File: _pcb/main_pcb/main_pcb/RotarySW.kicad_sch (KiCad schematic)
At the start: 28 parts

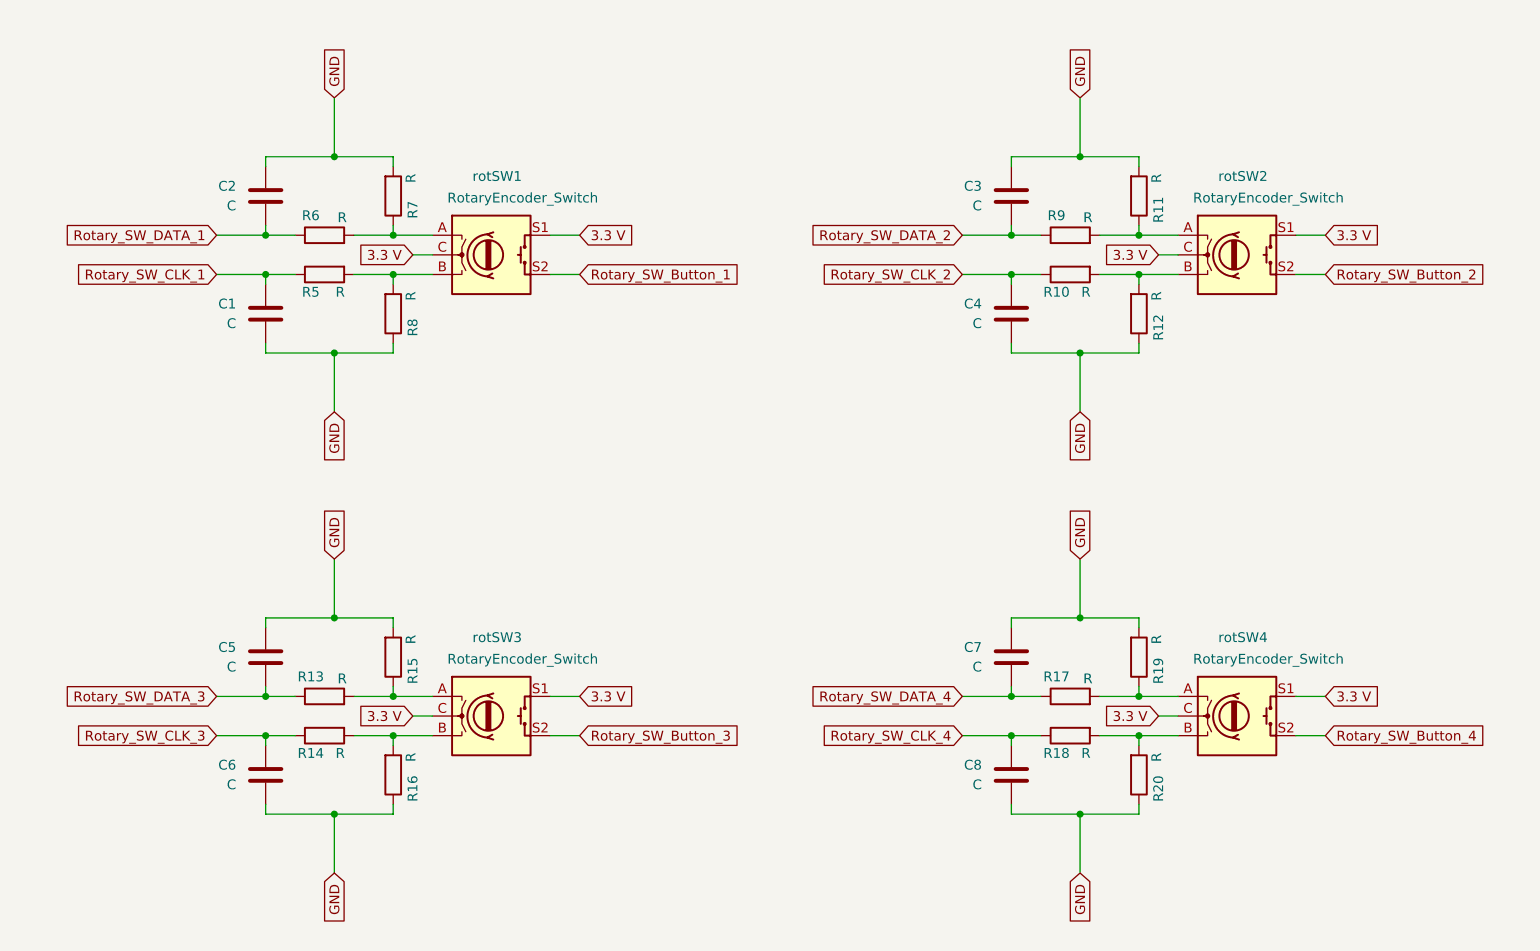
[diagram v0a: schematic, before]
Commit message: rewired rot sw curcits to new plans reduced to only 3
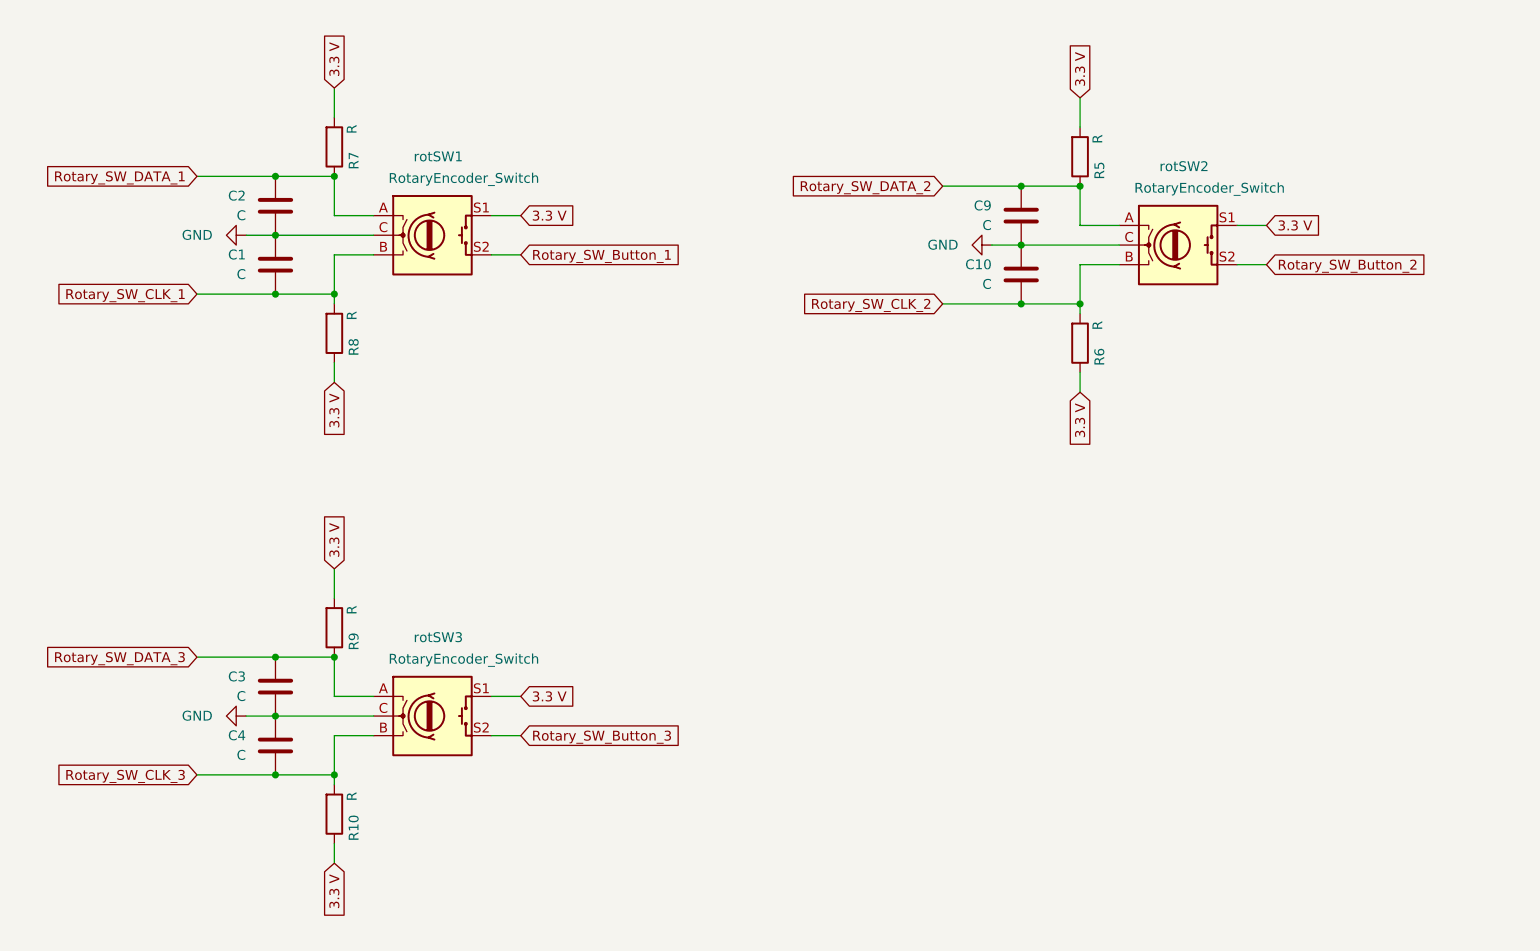
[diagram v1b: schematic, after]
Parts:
- removed C5, C6, C7, C8: C, Capacitor_SMD:C_1206_3216Metric, symbol Device:C
- removed R11, R12, R13, R14, R15, R16, R17, R18, R19, R20: R, Resistor_SMD:R_1206_3216Metric, symbol Device:R
- removed rotSW4: RotaryEncoder_Switch, Rotary_Encoder:RotaryEncoder_Alps_EC11E-Switch_Vertical_H20mm, symbol Device:RotaryEncoder_Switch
- added C10, C9: C, Capacitor_SMD:C_1206_3216Metric, symbol Device:C
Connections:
- net 3.3 V: now also R10.1, R5.2, R6.1, R7.2, R8.1, R9.2; no longer rotSW1.C, rotSW2.C, rotSW3.C
- net GND: now also C1.1, C2.2, C3.2, C4.1, rotSW1.C, rotSW2.C, rotSW3.C, C10.1, C9.2; no longer C1.2, C2.1, C3.1, C4.2, R7.2, R8.1
- net Rotary_SW_CLK_1: now also C1.2, R8.2, rotSW1.B; no longer C1.1, R5.1
- net Rotary_SW_CLK_2: now also R6.2, rotSW2.B, C10.2; no longer C4.1, R10.1
- net Rotary_SW_CLK_3: now also C4.2, R10.2, rotSW3.B
- net Rotary_SW_DATA_1: now also C2.1, R7.1, rotSW1.A; no longer C2.2, R6.1
- net Rotary_SW_DATA_2: now also R5.1, rotSW2.A, C9.1; no longer C3.2, R9.1
- net Rotary_SW_DATA_3: now also C3.1, R9.1, rotSW3.A
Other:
- moved on the sheet: C2, R7, R8, rotSW1, rotSW2, rotSW3
